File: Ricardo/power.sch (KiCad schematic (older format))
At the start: 31 parts, among them J11 Conn_01x02_Male, U8 TPS63031

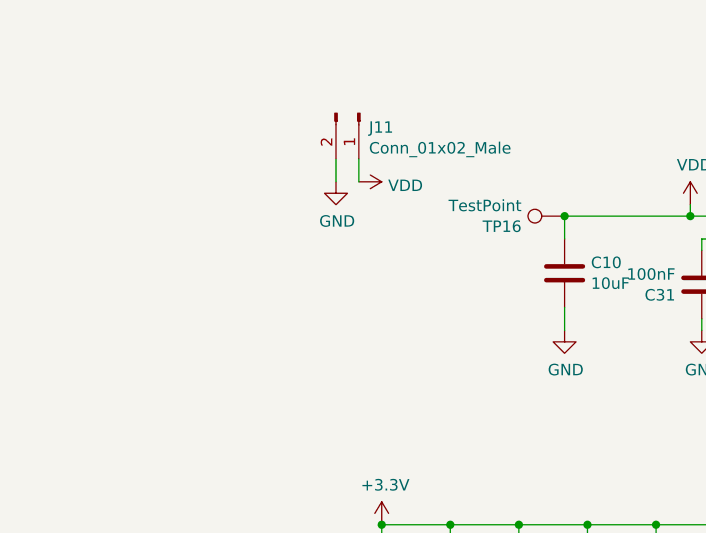
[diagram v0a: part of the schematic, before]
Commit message: RICARDO-V3 added power through usb, fixed issue with power plane on layer3
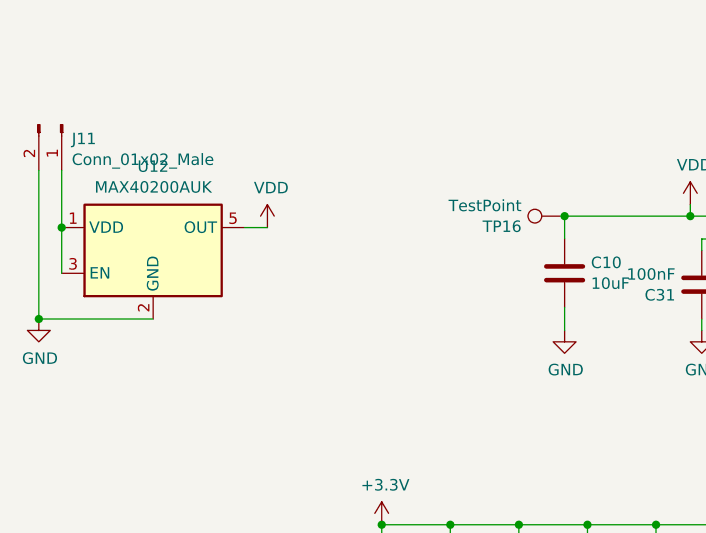
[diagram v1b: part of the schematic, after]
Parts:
- added U12: MAX40200AUK, Package_TO_SOT_SMD:SOT-23-5, symbol Analog_Switch:MAX40200AUK
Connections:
- net GND: now also U12.2 (GND)
- net VDD: now also U12.5 (OUT); no longer J11.1 (Pin_1)
- new net: J11.1 (Pin_1), U12.1 (VDD), U12.3 (EN)
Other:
- moved on the sheet: J11
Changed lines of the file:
@@
 L Connector:Conn_01x02_Male J11
 U 1 1 5DE7E179
-P 3700 3350
-F 0 "J11" V 3762 3394 50  0000 L CNN
-F 1 "Conn_01x02_Male" V 3853 3394 50  0000 L CNN
-F 2 "Connector_JST:JST_PH_S2B-PH-K_1x02_P2.00mm_Horizontal" H 3700 3350 50  0001 C CNN
-F 3 "~" H 3700 3350 50  0001 C CNN
-	1    3700 3350
+P 2400 3400
+F 0 "J11" V 2462 3444 50  0000 L CNN
+F 1 "Conn_01x02_Male" V 2553 3444 50  0000 L CNN
+F 2 "Connector_JST:JST_PH_S2B-PH-K_1x02_P2.00mm_Horizontal" H 2400 3400 50  0001 C CNN
+F 3 "~" H 2400 3400 50  0001 C CNN
+	1    2400 3400
 	0    1    1    0
 $EndComp
-$Comp
-L power:VDD #PWR062
-U 1 1 5DE7F5AD
-P 3700 3650
-F 0 "#PWR062" H 3700 3500 50  0001 C CNN
-F 1 "VDD" V 3717 3778 50  0000 L CNN
-F 2 "" H 3700 3650 50  0001 C CNN
-F 3 "" H 3700 3650 50  0001 C CNN
-	1    3700 3650
-	0    1    1    0
-$EndComp
-Wire Wire Line
-	3700 3550 3700 3650
 $Comp
 L power:GND #PWR059
 U 1 1 5DE8310C
-P 3600 3650
-F 0 "#PWR059" H 3600 3400 50  0001 C CNN
-F 1 "GND" H 3605 3477 50  0000 C CNN
-F 2 "" H 3600 3650 50  0001 C CNN
-F 3 "" H 3600 3650 50  0001 C CNN
-	1    3600 3650
-	1    0    0    -1
-$EndComp
-Wire Wire Line
-	3600 3650 3600 3550
+P 2300 4250
+F 0 "#PWR059" H 2300 4000 50  0001 C CNN
+F 1 "GND" H 2305 4077 50  0000 C CNN
+F 2 "" H 2300 4250 50  0001 C CNN
+F 3 "" H 2300 4250 50  0001 C CNN
+	1    2300 4250
+	1    0    0    -1
+$EndComp
 Wire Wire Line
 	8250 5250 8250 5150
@@
 Wire Wire Line
 	6050 4700 6550 4700
+$Comp
+L Analog_Switch:MAX40200AUK U12
+U 1 1 5E63069C
+P 2800 3950
+F 0 "U12" H 2800 4317 50  0000 C CNN
+F 1 "MAX40200AUK" H 2800 4226 50  0000 C CNN
+F 2 "Package_TO_SOT_SMD:SOT-23-5" H 2800 4450 50  0001 C CNN
+F 3 "https://datasheets.maximintegrated.com/en/ds/MAX40200.pdf" H 2800 4450 50  0001 C CNN
+	1    2800 3950
+	1    0    0    -1
+$EndComp
+Wire Wire Line
+	2400 3600 2400 3850
+Wire Wire Line
+	2400 3850 2400 4050
+Connection ~ 2400 3850
+Wire Wire Line
+	2300 4250 2800 4250
+Wire Wire Line
+	2300 3600 2300 4250
+Connection ~ 2300 4250
+$Comp
+L power:VDD #PWR054
+U 1 1 5E65F78E
+P 3300 3850
+F 0 "#PWR054" H 3300 3700 50  0001 C CNN
+F 1 "VDD" H 3317 4023 50  0000 C CNN
+F 2 "" H 3300 3850 50  0001 C CNN
+F 3 "" H 3300 3850 50  0001 C CNN
+	1    3300 3850
+	1    0    0    -1
+$EndComp
+Wire Wire Line
+	3300 3850 3200 3850
 $EndSCHEMATC
